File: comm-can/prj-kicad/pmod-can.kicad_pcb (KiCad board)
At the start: 2 copper layers, 0 parts

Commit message: Comm-CAN: Generate netlist
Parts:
- added C1, C4, C5: 10uF, comm-can:SMD0805, F.Cu at (148.5, 105.0)
- added C2, C3, C6: 100nF, comm-can:SMD0603, F.Cu at (148.5, 105.0)
- added C7: C, comm-can:SMD0603, F.Cu at (148.5, 105.0)
- added J1: JUMPER, comm-can:CONN_2, F.Cu at (148.5, 105.0)
- added L1: 4,7uH, comm-can:I_EPL3010, F.Cu at (148.5, 105.0)
- added P1: PMOD, comm-can:CONN_PMOD-Male, F.Cu at (148.5, 105.0)
- added P2: CONN_3, comm-can:CONN_MC000035, F.Cu at (148.5, 105.0)
- added R1: R, comm-can:SMD1206, F.Cu at (148.5, 105.0)
- added R2, R5, R6, R8: R, comm-can:SMD0603, F.Cu at (148.5, 105.0)
- added R3, R4: 0, comm-can:SMD0402, F.Cu at (148.5, 105.0)
- added R7: 0, comm-can:SMD0603, F.Cu at (148.5, 105.0)
- added TP2, TP3, TP4: CONN_1, comm-can:TP_SMD, F.Cu at (148.5, 105.0)
- added U1: MCP2562, comm-can:SOIC-8E, F.Cu at (148.5, 105.0)
- added U2: MCP2515-ST, comm-can:TSSOP20, F.Cu at (148.5, 105.0)
- added U3: TLV61220, comm-can:SOT23-6, F.Cu at (148.5, 105.0)
- added X1: 8MHz, comm-can:Q_DFN3225, F.Cu at (148.5, 105.0)

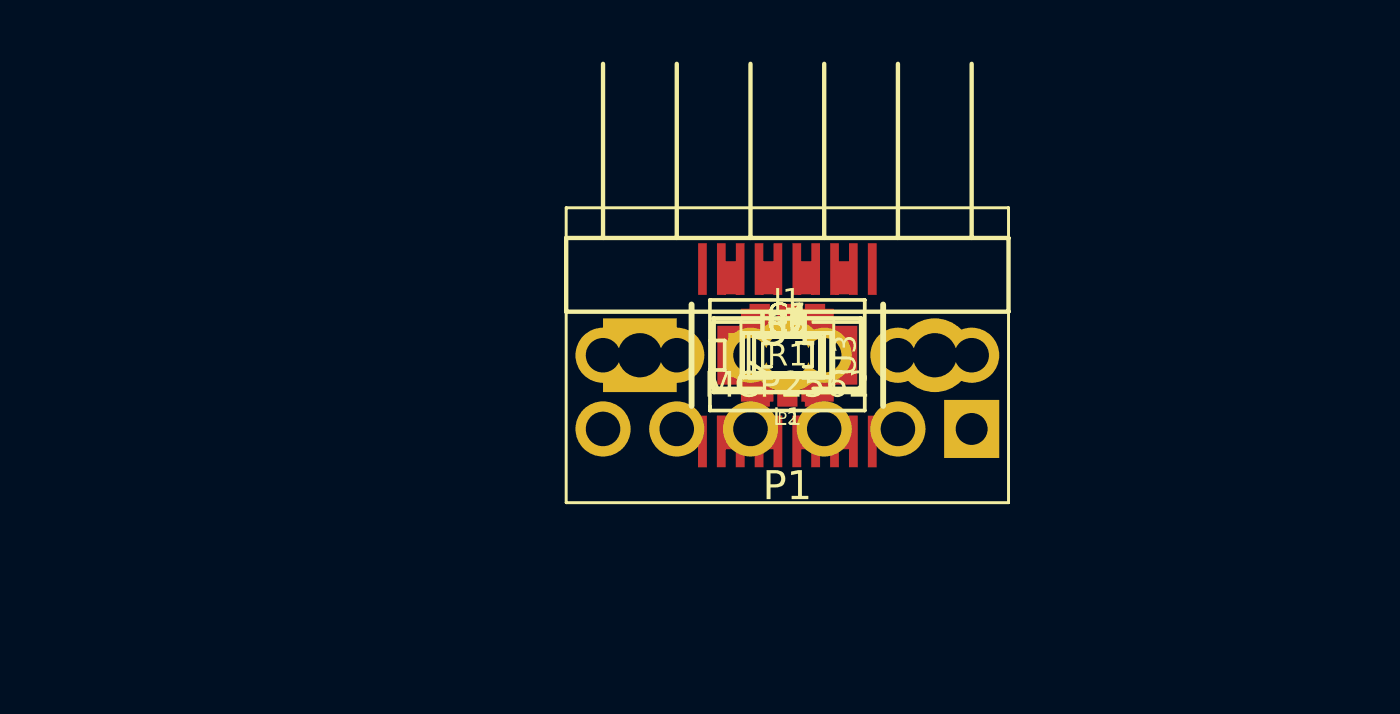
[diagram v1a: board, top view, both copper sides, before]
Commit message: Comm-CAN: Update board routing
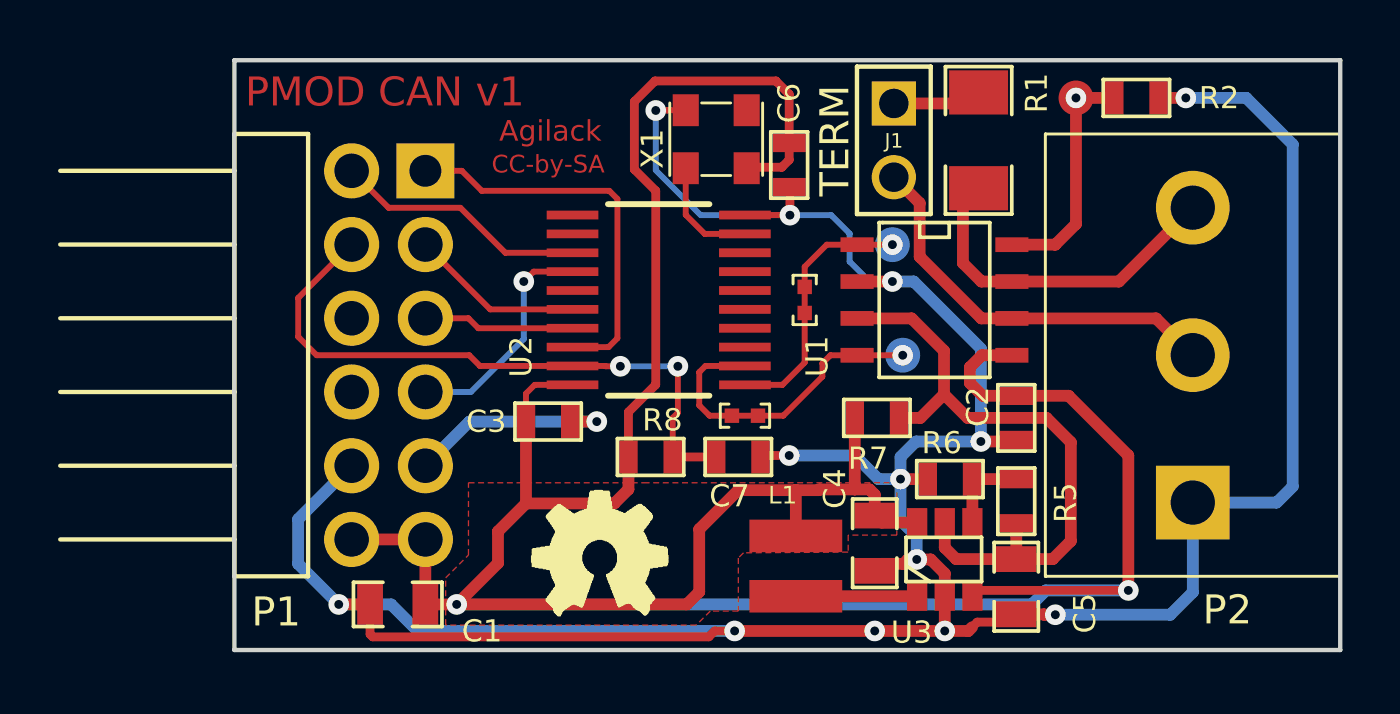
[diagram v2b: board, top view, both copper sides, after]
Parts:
- added logo_ohw: VAL**, comm-can:logo-ohw, F.Cu at (142.0, 112.0)
- TP2, TP3: moved to B.Cu
- moved C1 15.9 mm to (135.1, 113.6), turned to 180 degrees
- moved P1 15.0 mm to (133.5, 105.0), turned to 90 degrees
- moved R2 14.9 mm to (160.5, 96.1)
- moved P2 14.0 mm to (162.5, 105.0), turned to 90 degrees
- moved TP4 13.3 mm to (158.4, 96.1)
- moved C5 11.2 mm to (156.4, 113.0), turned to 270 degrees
- moved R1 9.91 mm to (155.1, 97.6), turned to 90 degrees
- moved R5 9.35 mm to (156.4, 110.0), turned to 90 degrees
- moved U3 8.88 mm to (153.9, 112.0)
- moved C3 8.55 mm to (140.3, 107.3)
- moved J1 8.26 mm to (152.2, 97.6), turned to 270 degrees
- moved C2 8.18 mm to (156.4, 107.2), turned to 270 degrees
- moved X1 7.84 mm to (146.1, 97.6), turned to 180 degrees
- moved L1 7.27 mm to (148.8, 112.3), turned to 270 degrees
- moved C4 7.14 mm to (151.5, 111.5), turned to 270 degrees
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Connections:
- net Net-(J1-Pad2) renamed /CAN_H
- net Net-(P2-Pad3) renamed /CAN_L
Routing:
- net GND: track 0.00 -> 126.0 mm, vias 0 -> 14
- net VCC: track 0.00 -> 109.1 mm, vias 0 -> 2
- net 5V: track 0.00 -> 22.2 mm
- net RST: track 0.00 -> 22.1 mm, vias 0 -> 2
- net /CAN_H: track 0.00 -> 13.9 mm
- net SPI_CS: track 0.00 -> 13.5 mm
- net /CAN_L: track 0.00 -> 12.0 mm
- net CAN_RX: track 0.00 -> 11.1 mm, vias 0 -> 1
- net CAN_TX: track 0.00 -> 9.01 mm, vias 0 -> 1
- net SPI_INT: track 0.00 -> 8.78 mm
- net Net-(R2-Pad1): track 0.00 -> 8.17 mm, vias 0 -> 1
- net SPI_SCK: track 0.00 -> 7.95 mm, vias 0 -> 1
- net SPI_MOSI: track 0.00 -> 5.99 mm
- net SPI_MISO: track 0.00 -> 5.21 mm
- net Net-(L1-Pad2): track 0.00 -> 4.18 mm
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- added copper zone on B.Cu, net GND
- added copper zone on F.Cu, net VCC
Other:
- board outline added: 38.1 x 20.3 mm
- net class Default: trace_width 0.25 -> 0.2032
- rule pad_to_mask_clearance: 0 -> 0.2
- rule trace_min: 0.2 -> 0.15
- board text added: "Agilack"
- board text added: "CC-by-SA"
- board text added: "PMOD CAN v1"
- board text added: "TERM"
